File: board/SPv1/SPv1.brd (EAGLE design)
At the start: 114 x 27.9 mm, 72 parts, among them IC1 S34ML0XG1, IC2 F55[0/1]X---PT48, IC3 S34ML0XG1, IC4 74LS14D, IC5 F55[0/1]X---PT48, IC6 74LS14D, Q1 12MHz, Q2 12MHz

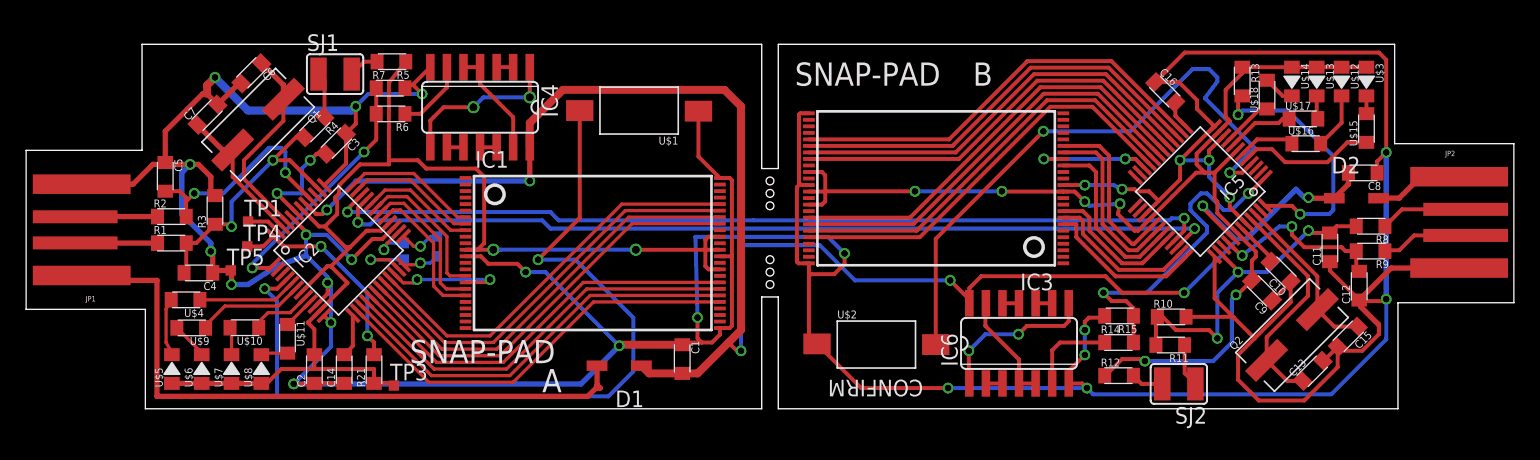
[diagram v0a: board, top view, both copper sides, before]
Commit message: fixes to board (connector; PUR line)
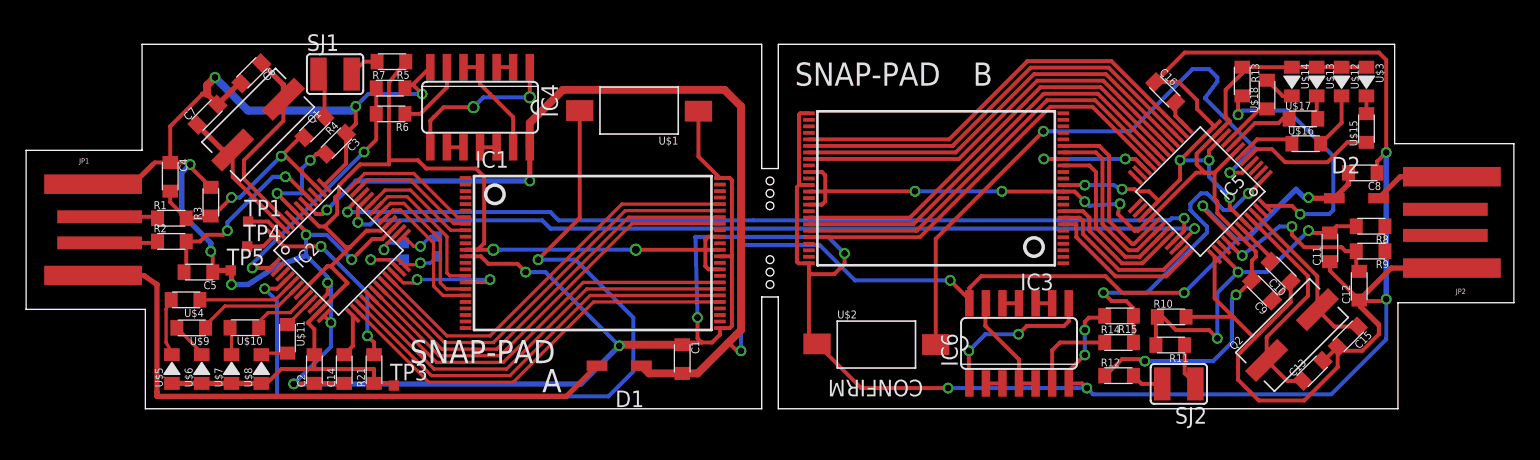
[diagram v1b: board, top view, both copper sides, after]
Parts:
- moved C5 7.73 mm to (12.7, 16.8), turned to 180 degrees
- moved C4 7.68 mm to (10.5, 24.1), turned to 270 degrees
- moved R2 1.91 mm to (10.7, 19.2)
- moved R1 1.90 mm to (10.7, 21.0)
- moved JP1 1.27 mm to (4.83, 20.1), turned to 0 degrees
- moved JP2 0.95 mm to (108.6, 20.6), turned to 180 degrees
- moved R3 0.71 mm to (13.7, 22.2)
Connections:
- removed net N$11: R4.P$2, SJ1.1
- removed net N$32: R11.P$2, SJ2.1
- net PUR_A: now also R4.P$2, SJ1.1
- net PUR_B: now also R11.P$2, SJ2.1
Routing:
- net N$12: track 6.72 -> 0.00 mm
- net N$13: track 6.68 -> 0.00 mm
- net PUR_A: track 0.00 -> 3.48 mm
- net N$11: track 3.48 -> 0.00 mm
- net PUR_B: track 0.00 -> 3.32 mm
- net N$32: track 3.32 -> 0.00 mm
- net GND: track 407.8 -> 405.0 mm
- net N$33: track 50.9 -> 48.4 mm
- net D+_A: track 20.5 -> 18.2 mm
- net D-_A: track 17.1 -> 15.1 mm
- net N$2: track 6.32 -> 4.49 mm
- net N$1: track 6.32 -> 4.49 mm
- net N$40: track 6.85 -> 6.30 mm

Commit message: route board changes
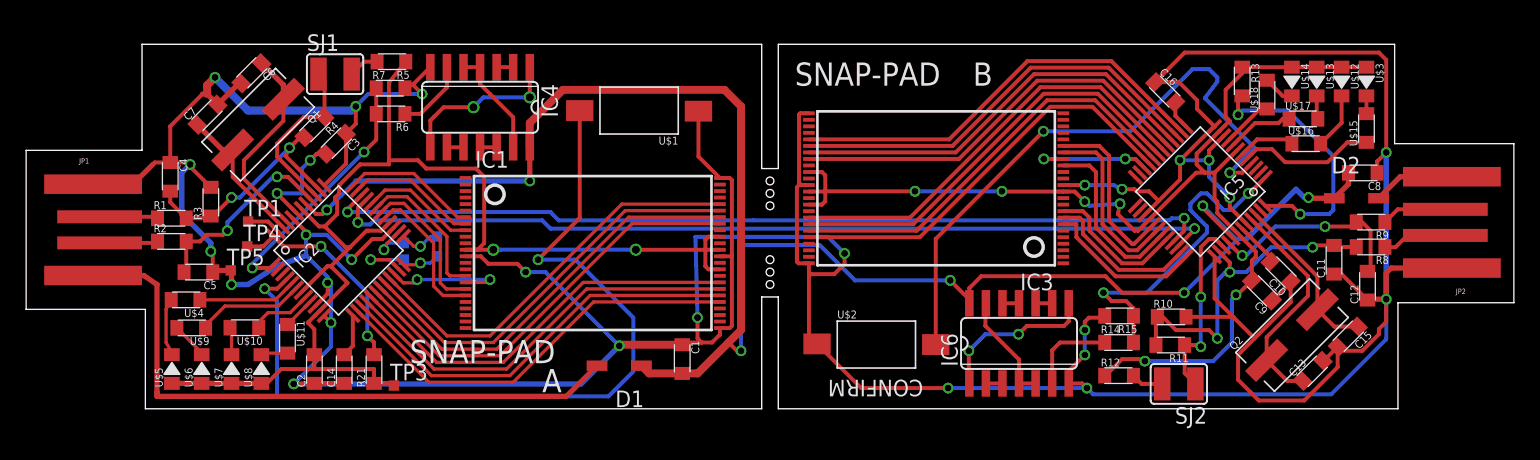
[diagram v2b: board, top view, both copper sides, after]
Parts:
- moved R9 2.22 mm to (102.6, 20.7)
- moved R8 1.59 mm to (102.6, 18.8)
- moved C11 1.00 mm to (99.7, 17.8)
- moved C12 0.63 mm to (102.3, 15.8)
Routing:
- net PUR_B: track 3.32 -> 14.5 mm, vias 0 -> 2
- net PUR_A: track 3.48 -> 13.1 mm
- net GND: track 405.0 -> 399.4 mm
- net N$13: track 0.00 -> 5.04 mm
- net N$12: track 0.00 -> 5.02 mm
- net D-_B: track 13.8 -> 15.8 mm
